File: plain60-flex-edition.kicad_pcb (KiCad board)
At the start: 2 copper layers, 284.7 x 94.2 mm, 175 parts, among them J1 HRO-TYPE-C-31-M-12, J2 ISP, J3 ai03_ud, K1 KEYSW, K10 KEYSW, K11 KEYSW, K12 KEYSW, K13 KEYSW, K14 KEYSW, K15 KEYSW, K15-1 KEYSW, K16 KEYSW, K17 KEYSW, K18 KEYSW, K19 KEYSW, K2 KEYSW, K20 KEYSW, K21 KEYSW, K22 KEYSW, K23 KEYSW, K24 KEYSW, K25 KEYSW, K26 KEYSW, K27 KEYSW, K28 KEYSW, K29 KEYSW, K3 KEYSW, K31 KEYSW, K31-1 KEYSW, K32 KEYSW, K33 KEYSW, K34 KEYSW, K35 KEYSW, K36 KEYSW, K37 KEYSW, K38 KEYSW, K39 KEYSW, K4 KEYSW, K40 KEYSW, K41 KEYSW, K42 KEYSW, K43 KEYSW, K44 KEYSW, K44-1 KEYSW, K46 KEYSW, K46-1 KEYSW, K47 KEYSW, K48 KEYSW, K49 KEYSW, K5 KEYSW, K50 KEYSW, K51 KEYSW, K52 KEYSW, K53 KEYSW, K54 KEYSW, K55 KEYSW, K56 KEYSW, K57 KEYSW, K58 KEYSW, K58-1 KEYSW, K59 KEYSW, K6 KEYSW, K61 KEYSW, K61-1 KEYSW, K62 KEYSW, K62-1 KEYSW, K63 KEYSW, K63-1 KEYSW, K67 KEYSW, K67-1 KEYSW, K7 KEYSW, K71 KEYSW, K72 KEYSW, K72-1 KEYSW, K73 KEYSW, K73-1 KEYSW, K74 KEYSW, K74-1 KEYSW, K8 KEYSW, K9 KEYSW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

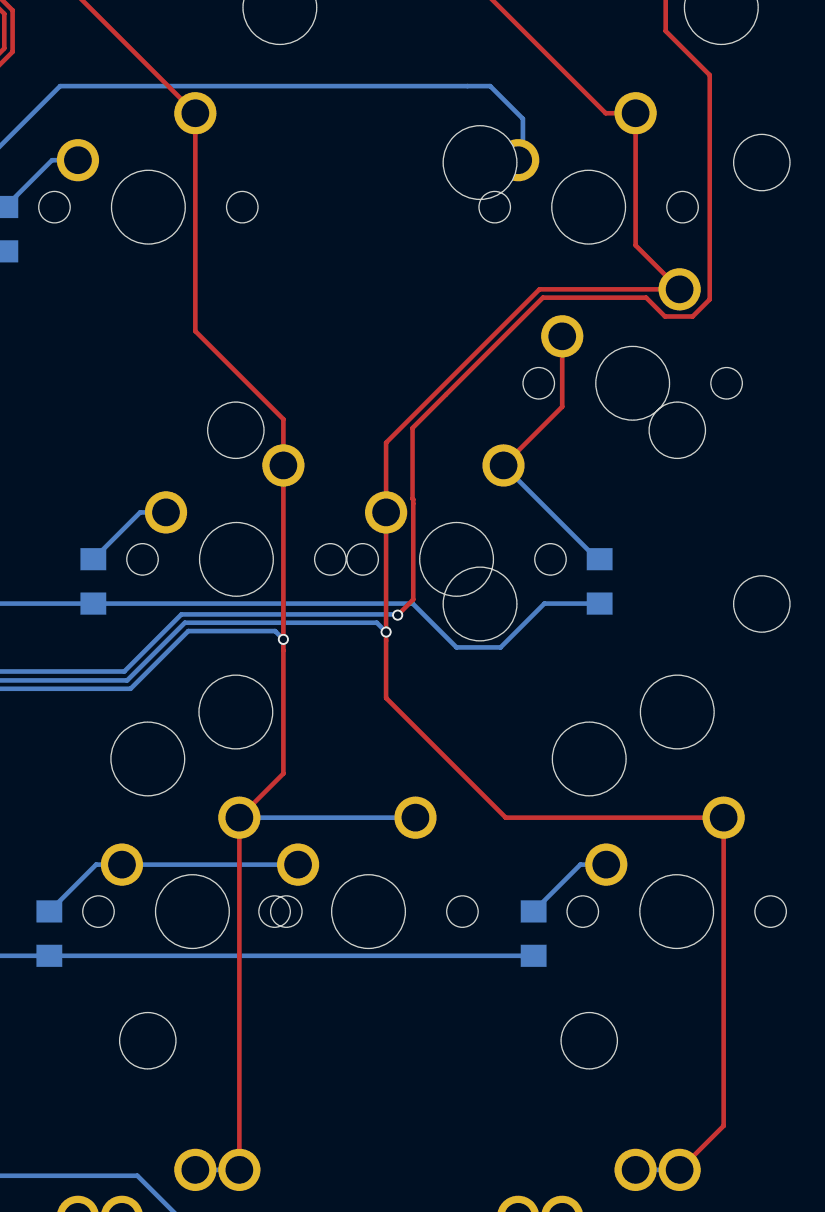
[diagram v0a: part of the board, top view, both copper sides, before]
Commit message: Rotate enter stabilizer, not shift
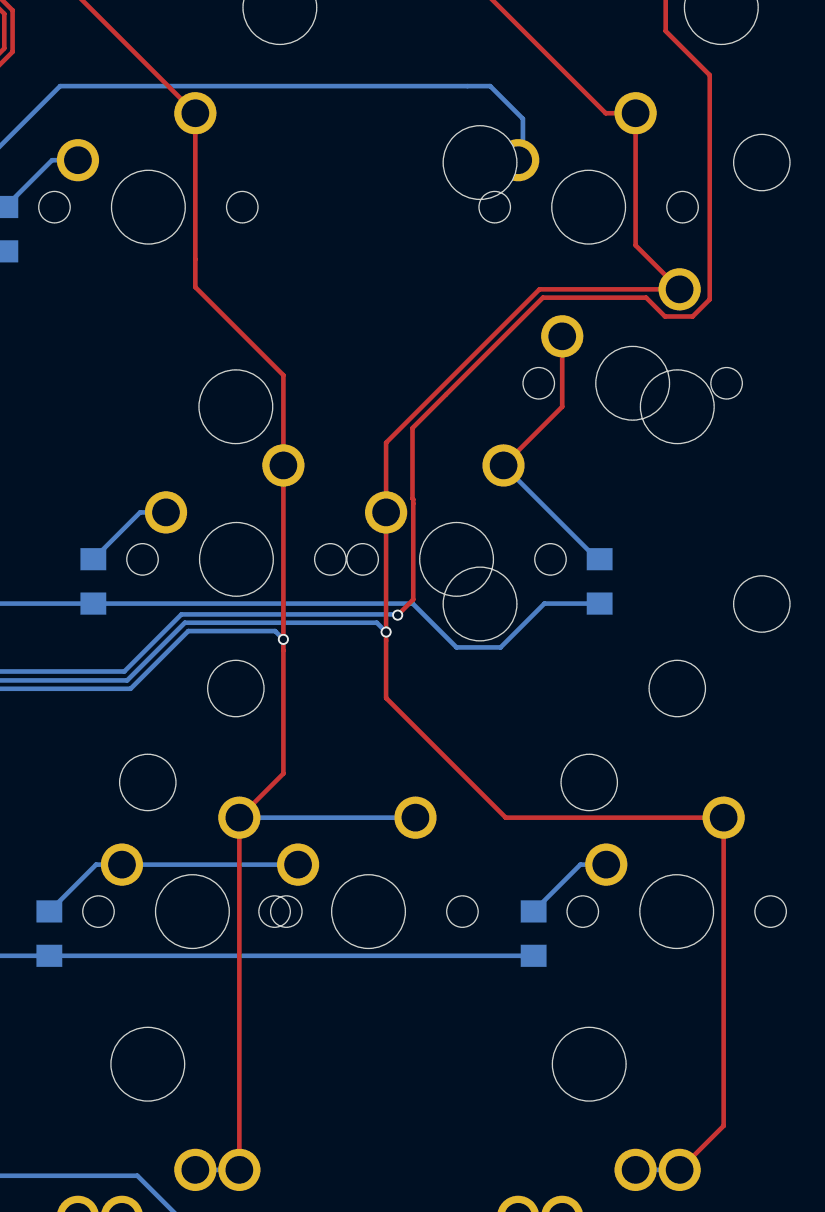
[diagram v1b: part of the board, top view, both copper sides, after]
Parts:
- K44: footprint Keeb_switches:CHERRY_PCB_225H -> Keeb_switches:CHERRY_PCB_225H_F
- K58: footprint Keeb_switches:CHERRY_PCB_275H_F -> Keeb_switches:CHERRY_PCB_275H
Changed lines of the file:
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@@
     (thickness 1.6)
     (drawings 62)
-    (tracks 1160)
+    (tracks 1161)
     (modules 175)
     (nets 107)
@@
     (add_net "Net-(H1-Pad1)")
     (add_net "Net-(J1-Pad10)")
+    (add_net "Net-(J1-Pad3)")
     (add_net "Net-(J1-Pad4)")
+    (add_net "Net-(J1-Pad9)")
     (add_net "Net-(LS1-Pad1)")
     (add_net "Net-(R1-Pad1)")
@@
     (add_net "Net-(U1-Pad16)")
     (add_net "Net-(U1-Pad17)")
+    (add_net "Net-(U1-Pad42)")
     (add_net "RST")
     (add_net "SCK")
@@
     (add_net "VCC")
   )
-  (module "Keeb_switches:CHERRY_PCB_275H_F" (layer "F.Cu")
+  (module "Keeb_switches:CHERRY_PCB_275H" (layer "F.Cu")
     (at 259.556468 66.675)
     (fp_text reference "K58" (at 0 3.175) (layer "F.SilkS") hide
@@
       (effects (font (size 1.524 1.524) (thickness 0.3048)) (justify left))
     )
+    (pad "HOLE" np_thru_hole circle (at 11.938 8.255) (size 3.9878 3.9878) (drill 3.9878) (layers *.Cu *.Mask))
+    (pad "HOLE" np_thru_hole circle (at -11.938 8.255) (size 3.9878 3.9878) (drill 3.9878) (layers *.Cu *.Mask))
+    (pad "HOLE" np_thru_hole circle (at 11.938 -6.985) (size 3.048 3.048) (drill 3.048) (layers *.Cu *.Mask))
+    (pad "HOLE" np_thru_hole circle (at -11.938 -6.985) (size 3.048 3.048) (drill 3.048) (layers *.Cu *.Mask))
+    (pad "HOLE" np_thru_hole circle (at 5.08 0) (size 1.7018 1.7018) (drill 1.7018) (layers *.Cu *.Mask))
+    (pad "HOLE" np_thru_hole circle (at -5.08 0) (size 1.7018 1.7018) (drill 1.7018) (layers *.Cu *.Mask))
+    (pad "HOLE" np_thru_hole circle (at 0 0) (size 3.9878 3.9878) (drill 3.9878) (layers *.Cu *.Mask))
+    (pad "2" thru_hole circle (at -3.81 -2.54) (size 2.286 2.286) (drill 1.4986) (layers *.Cu *.Mask)
+      (net 62 "Net-(D58-Pad2)"))
+    (pad "1" thru_hole circle (at 2.54 -5.08) (size 2.286 2.286) (drill 1.4986) (layers *.Cu *.Mask)
+      (net 87 "col12"))
+  )
+  (module "Keeb_switches:CHERRY_PCB_225H_F" (layer "F.Cu")
+    (at 264.31875 47.625)
+    (fp_text reference "K44" (at 0 3.175) (layer "F.SilkS") hide
+      (effects (font (size 1.27 1.524) (thickness 0.2032)))
+    )
+    (fp_text value "KEYSW" (at 0 5.08) (layer "F.SilkS") hide
+      (effects (font (size 1.27 1.524) (thickness 0.2032)))
+    )
+    (fp_line (start -21.43125 9.525) (end -21.43125 -9.525) (layer "Dwgs.User") (width 0.1524))
+    (fp_line (start 21.43125 9.525) (end -21.43125 9.525) (layer "Dwgs.User") (width 0.1524))
+    (fp_line (start 21.43125 -9.525) (end 21.43125 9.525) (layer "Dwgs.User") (width 0.1524))
+    (fp_line (start -21.43125 -9.525) (end 21.43125 -9.525) (layer "Dwgs.User") (width 0.1524))
+    (fp_line (start -6.35 6.35) (end -6.35 -6.35) (layer "Cmts.User") (width 0.1524))
+    (fp_line (start 6.35 6.35) (end -6.35 6.35) (layer "Cmts.User") (width 0.1524))
+    (fp_line (start 6.35 -6.35) (end 6.35 6.35) (layer "Cmts.User") (width 0.1524))
+    (fp_line (start -6.35 -6.35) (end 6.35 -6.35) (layer "Cmts.User") (width 0.1524))
+    (fp_text user "2.25u" (at -21.43125 8.334375) (layer "Dwgs.User")
+      (effects (font (size 1.524 1.524) (thickness 0.3048)) (justify left))
+    )
     (pad "" np_thru_hole circle (at 11.938 -8.255) (size 3.9878 3.9878) (drill 3.9878) (layers *.Cu *.Mask))
     (pad "" np_thru_hole circle (at -11.938 -8.255) (size 3.9878 3.9878) (drill 3.9878) (layers *.Cu *.Mask))
@@
     (pad "HOLE" np_thru_hole circle (at 0 0) (size 3.9878 3.9878) (drill 3.9878) (layers *.Cu *.Mask))
     (pad "2" thru_hole circle (at -3.81 -2.54) (size 2.286 2.286) (drill 1.4986) (layers *.Cu *.Mask)
-      (net 62 "Net-(D58-Pad2)"))
+      (net 88 "col13"))
     (pad "1" thru_hole circle (at 2.54 -5.08) (size 2.286 2.286) (drill 1.4986) (layers *.Cu *.Mask)
-      (net 87 "col12"))
+      (net 48 "Net-(D44-Pad2)"))
   )
   (module "Keeb_switches:CHERRY_PLATE_100H" (layer "F.Cu")
@@
       (net 50 "Net-(D46-Pad2)"))
   )
-  (module "Keeb_switches:CHERRY_PCB_225H" (layer "F.Cu")
-    (at 264.31875 47.625)
-    (fp_text reference "K44" (at 0 3.175) (layer "F.SilkS") hide
-      (effects (font (size 1.27 1.524) (thickness 0.2032)))
-    )
-    (fp_text value "KEYSW" (at 0 5.08) (layer "F.SilkS") hide
-      (effects (font (size 1.27 1.524) (thickness 0.2032)))
-    )
-    (fp_line (start -21.43125 9.525) (end -21.43125 -9.525) (layer "Dwgs.User") (width 0.1524))
-    (fp_line (start 21.43125 9.525) (end -21.43125 9.525) (layer "Dwgs.User") (width 0.1524))
-    (fp_line (start 21.43125 -9.525) (end 21.43125 9.525) (layer "Dwgs.User") (width 0.1524))
-    (fp_line (start -21.43125 -9.525) (end 21.43125 -9.525) (layer "Dwgs.User") (width 0.1524))
-    (fp_line (start -6.35 6.35) (end -6.35 -6.35) (layer "Cmts.User") (width 0.1524))
-    (fp_line (start 6.35 6.35) (end -6.35 6.35) (layer "Cmts.User") (width 0.1524))
-    (fp_line (start 6.35 -6.35) (end 6.35 6.35) (layer "Cmts.User") (width 0.1524))
-    (fp_line (start -6.35 -6.35) (end 6.35 -6.35) (layer "Cmts.User") (width 0.1524))
-    (fp_text user "2.25u" (at -17.62252 8.255) (layer "Dwgs.User")
-      (effects (font (size 1.524 1.524) (thickness 0.3048)))
-    )
-    (pad "HOLE" np_thru_hole circle (at 11.938 8.255) (size 3.9878 3.9878) (drill 3.9878) (layers *.Cu *.Mask))
-    (pad "HOLE" np_thru_hole circle (at -11.938 8.255) (size 3.9878 3.9878) (drill 3.9878) (layers *.Cu *.Mask))
-    (pad "HOLE" np_thru_hole circle (at 11.938 -6.985) (size 3.048 3.048) (drill 3.048) (layers *.Cu *.Mask))
-    (pad "HOLE" np_thru_hole circle (at -11.938 -6.985) (size 3.048 3.048) (drill 3.048) (layers *.Cu *.Mask))
-    (pad "HOLE" np_thru_hole circle (at 5.08 0) (size 1.7018 1.7018) (drill 1.7018) (layers *.Cu *.Mask))
-    (pad "HOLE" np_thru_hole circle (at -5.08 0) (size 1.7018 1.7018) (drill 1.7018) (layers *.Cu *.Mask))
-    (pad "HOLE" np_thru_hole circle (at 0 0) (size 3.9878 3.9878) (drill 3.9878) (layers *.Cu *.Mask))
-    (pad "2" thru_hole circle (at -3.81 -2.54) (size 2.286 2.286) (drill 1.4986) (layers *.Cu *.Mask)
-      (net 88 "col13"))
-    (pad "1" thru_hole circle (at 2.54 -5.08) (size 2.286 2.286) (drill 1.4986) (layers *.Cu *.Mask)
-      (net 48 "Net-(D44-Pad2)"))
-  )
   (module "Keeb_switches:CHERRY_PLATE_100H" (layer "F.Cu")
     (at 252.4125 47.625)
@@
     (effects (font (size 2.5 2.5) (thickness 0.4)) (justify left mirror))
   )
+  (segment (start 250.19 23.495) (end 250.19 31.393049) (width 0.25) (layer "F.Cu") (net 87))
+  (segment (start 254.9525 37.663255) (end 250.19 32.900755) (width 0.25) (layer "F.Cu") (net 87))
+  (segment (start 254.9525 42.545) (end 254.9525 37.663255) (width 0.25) (layer "F.Cu") (net 87))
+  (segment (start 250.19 32.900755) (end 250.19 31.393049) (width 0.25) (layer "F.Cu") (net 87))
   (segment (start 23.217207 16.162513) (end 23.306269 16.162513) (width 0.25) (layer "B.Cu") (net 1))
   (segment (start 23.306269 16.162513) (end 23.81252 16.668764) (width 0.25) (layer "B.Cu") (net 1))
@@
   (segment (start 240.665 13.97) (end 250.19 23.495) (width 0.25) (layer "F.Cu") (net 87))
   (segment (start 240.665 4.445) (end 240.665 13.97) (width 0.25) (layer "F.Cu") (net 87))
-  (segment (start 250.19 35.282007) (end 254.9525 40.044507) (width 0.25) (layer "F.Cu") (net 87))
-  (segment (start 254.9525 40.044507) (end 254.9525 42.545) (width 0.25) (layer "F.Cu") (net 87))
-  (segment (start 250.19 23.495) (end 250.19 35.282007) (width 0.25) (layer "F.Cu") (net 87))
   (segment (start 254.9525 59.214016) (end 252.57146 61.595056) (width 0.25) (layer "F.Cu") (net 87))
   (segment (start 252.57146 80.64479) (end 252.57125 80.645) (width 0.25) (layer "F.Cu") (net 87))

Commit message: Update kicad version, fix outline export error, proper step file now!
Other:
- net class Default removed
- net class VCC removed
- board text removed: "+5v"

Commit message: Change website logo
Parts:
- G***: footprint Keeb_components:logo -> Keeb_components:logo_new
- moved G*** 5.73 mm to (70.5, 37.9)
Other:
- board text added: "based on Plain60 rev2.2"
- board text removed: "based on Plain60 rev2.1"
